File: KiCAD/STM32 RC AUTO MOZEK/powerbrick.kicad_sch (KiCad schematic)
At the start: 3 parts, among them J1 Conn_01x02_Socket, U1 LD1117S33TR_SOT223, U3 L7805

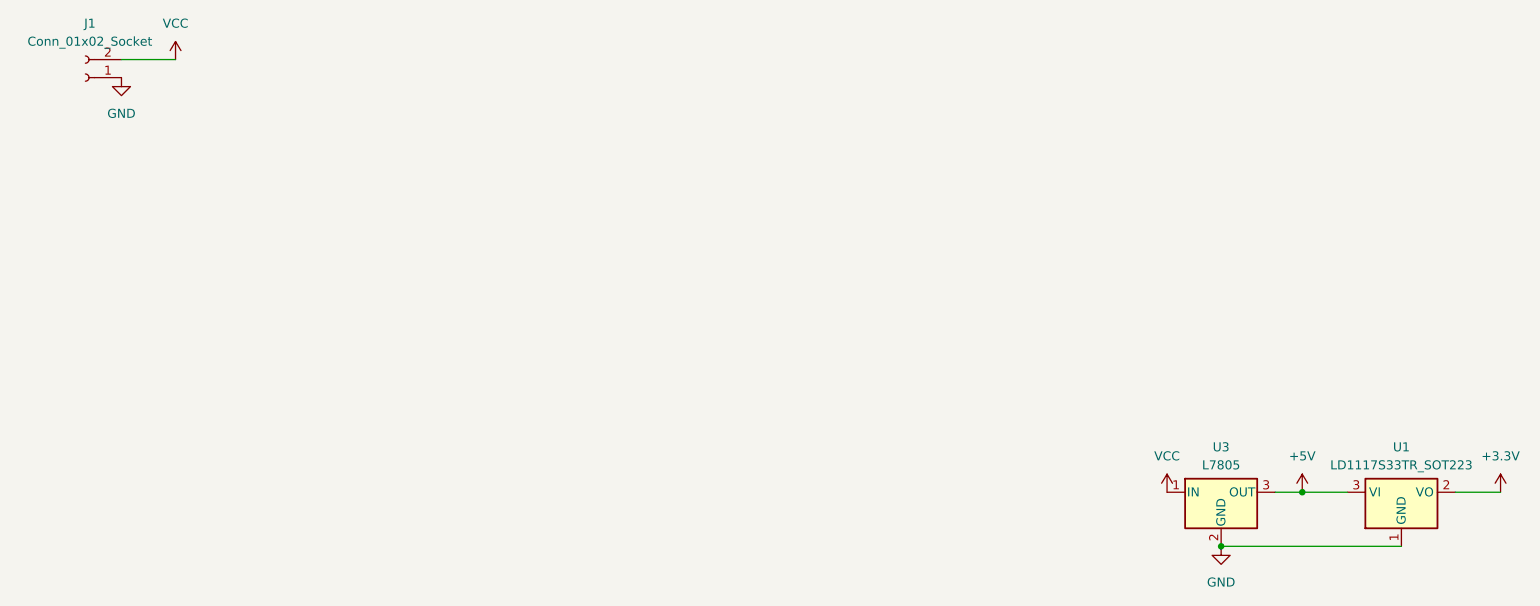
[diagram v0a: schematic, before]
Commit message: adding completation on schematic, working on board
need to add SWD Debug as input for programing
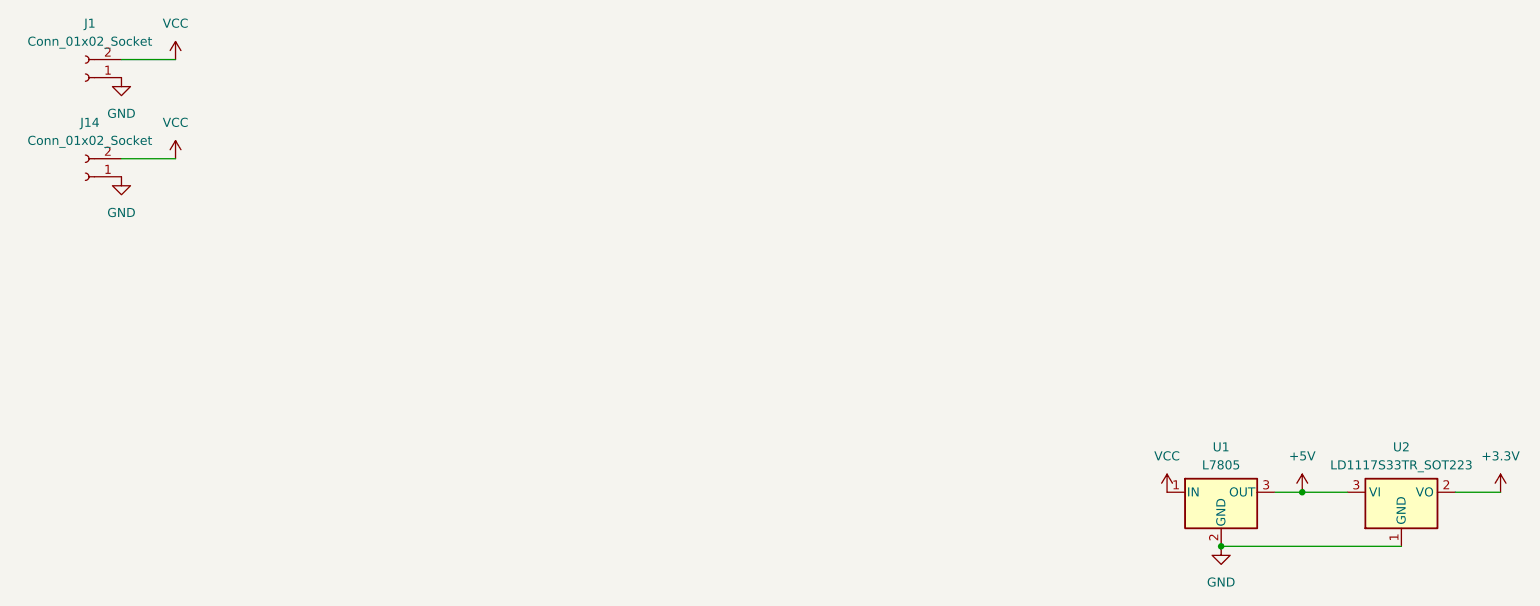
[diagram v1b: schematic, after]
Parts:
- added J14: Conn_01x02_Socket, Connector_Wire:SolderWire-2sqmm_1x02_P7.8mm_D2mm_OD3.9mm, symbol Connector:Conn_01x02_Socket
- J1: footprint Connector_Wire:SolderWire-2sqmm_1x02_P7.8mm_D2mm_OD3.9mm_Relief -> Connector_Wire:SolderWire-2sqmm_1x02_P7.8mm_D2mm_OD3.9mm
- renumbered U3 to U1, U1 to U2
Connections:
- net GND: now also J14.1 (Pin_1)
- net VCC: now also J14.2 (Pin_2)
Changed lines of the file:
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@@
+	(wire
+		(pts
+			(xy 35.56 34.29) (xy 27.94 34.29)
+		)
+		(stroke
+			(width 0)
+			(type default)
+		)
+	)
 	(wire
 		(pts
@@
 	)
 	(symbol
+		(lib_id "power:VCC")
+		(at 35.56 34.29 0)
+		(unit 1)
+		(exclude_from_sim no)
+		(in_bom yes)
+		(on_board yes)
+		(dnp no)
+		(fields_autoplaced yes)
+		(property "Reference" "#PWR086"
+			(at 35.56 38.1 0)
+			(effects
+				(font
+					(size 1.27 1.27)
+				)
+				(hide yes)
+			)
+		)
+		(property "Value" "VCC"
+			(at 35.56 29.21 0)
+			(effects
+				(font
+					(size 1.27 1.27)
+				)
+			)
+		)
+		(property "Footprint" ""
+			(at 35.56 34.29 0)
+			(effects
+				(font
+					(size 1.27 1.27)
+				)
+				(hide yes)
+			)
+		)
+		(property "Datasheet" ""
+			(at 35.56 34.29 0)
+			(effects
+				(font
+					(size 1.27 1.27)
+				)
+				(hide yes)
+			)
+		)
+		(property "Description" "Power symbol creates a global label with name \"VCC\""
+			(at 35.56 34.29 0)
+			(effects
+				(font
+					(size 1.27 1.27)
+				)
+				(hide yes)
+			)
+		)
+		(pin "1"
+		)
+		(instances
+			(project "STM32 RC AUTO MOZEK"
+				(path "/6e2a7673-a3dd-4427-9adf-f28c7cc113a0/dfd97a23-616e-451f-b7bb-3bcde87fded7"
+					(reference "#PWR086")
+					(unit 1)
+				)
+			)
+		)
+	)
+	(symbol
 		(lib_id "power:+5V")
 		(at 194.31 81.28 0)
@@
 		(dnp no)
 		(fields_autoplaced yes)
-		(property "Reference" "#PWR06"
+		(property "Reference" "#PWR05"
 			(at 194.31 85.09 0)
 			(effects
@@
 			(project ""
 				(path "/6e2a7673-a3dd-4427-9adf-f28c7cc113a0/dfd97a23-616e-451f-b7bb-3bcde87fded7"
-					(reference "#PWR06")
+					(reference "#PWR05")
 					(unit 1)
 				)
@@
 		(dnp no)
 		(fields_autoplaced yes)
-		(property "Reference" "U3"
+		(property "Reference" "U1"
 			(at 182.88 74.93 0)
 			(effects
@@
 			(project ""
 				(path "/6e2a7673-a3dd-4427-9adf-f28c7cc113a0/dfd97a23-616e-451f-b7bb-3bcde87fded7"
-					(reference "U3")
+					(reference "U1")
 					(unit 1)
 				)
@@
 		(dnp no)
 		(fields_autoplaced yes)
-		(property "Reference" "U1"
+		(property "Reference" "U2"
 			(at 208.28 74.93 0)
 			(effects
@@
 			(project ""
 				(path "/6e2a7673-a3dd-4427-9adf-f28c7cc113a0/dfd97a23-616e-451f-b7bb-3bcde87fded7"
-					(reference "U1")
+					(reference "U2")
+					(unit 1)
+				)
+			)
+		)
+	)
+	(symbol
+		(lib_id "power:GND")
+		(at 27.94 36.83 0)
+		(unit 1)
+		(exclude_from_sim no)
+		(in_bom yes)
+		(on_board yes)
+		(dnp no)
+		(fields_autoplaced yes)
+		(property "Reference" "#PWR085"
+			(at 27.94 43.18 0)
+			(effects
+				(font
+					(size 1.27 1.27)
+				)
+				(hide yes)
+			)
+		)
+		(property "Value" "GND"
+			(at 27.94 41.91 0)
+			(effects
+				(font
+					(size 1.27 1.27)
+				)
+			)
+		)
+		(property "Footprint" ""
+			(at 27.94 36.83 0)
+			(effects
+				(font
+					(size 1.27 1.27)
+				)
+				(hide yes)
+			)
+		)
+		(property "Datasheet" ""
+			(at 27.94 36.83 0)
+			(effects
+				(font
+					(size 1.27 1.27)
+				)
+				(hide yes)
+			)
+		)
+		(property "Description" "Power symbol creates a global label with name \"GND\" , ground"
+			(at 27.94 36.83 0)
+			(effects
+				(font
+					(size 1.27 1.27)
+				)
+				(hide yes)
+			)
+		)
+		(pin "1"
+		)
+		(instances
+			(project "STM32 RC AUTO MOZEK"
+				(path "/6e2a7673-a3dd-4427-9adf-f28c7cc113a0/dfd97a23-616e-451f-b7bb-3bcde87fded7"
+					(reference "#PWR085")
 					(unit 1)
 				)
@@
 		(dnp no)
 		(fields_autoplaced yes)
-		(property "Reference" "#PWR013"
+		(property "Reference" "#PWR03"
 			(at 175.26 85.09 0)
 			(effects
@@
 			(project "STM32 RC AUTO MOZEK"
 				(path "/6e2a7673-a3dd-4427-9adf-f28c7cc113a0/dfd97a23-616e-451f-b7bb-3bcde87fded7"
-					(reference "#PWR013")
+					(reference "#PWR03")
 					(unit 1)
 				)
@@
 		(dnp no)
 		(fields_autoplaced yes)
-		(property "Reference" "#PWR08"
+		(property "Reference" "#PWR02"
 			(at 35.56 24.13 0)
 			(effects
@@
 			(project ""
 				(path "/6e2a7673-a3dd-4427-9adf-f28c7cc113a0/dfd97a23-616e-451f-b7bb-3bcde87fded7"
-					(reference "#PWR08")
+					(reference "#PWR02")
 					(unit 1)
 				)
@@
 		(dnp no)
 		(fields_autoplaced yes)
-		(property "Reference" "#PWR09"
+		(property "Reference" "#PWR01"
 			(at 27.94 29.21 0)
 			(effects
@@
 			(project ""
 				(path "/6e2a7673-a3dd-4427-9adf-f28c7cc113a0/dfd97a23-616e-451f-b7bb-3bcde87fded7"
-					(reference "#PWR09")
+					(reference "#PWR01")
 					(unit 1)
 				)
@@
 		(dnp no)
 		(fields_autoplaced yes)
-		(property "Reference" "#PWR05"
+		(property "Reference" "#PWR06"
 			(at 222.25 85.09 0)
 			(effects
@@
 			(project ""
 				(path "/6e2a7673-a3dd-4427-9adf-f28c7cc113a0/dfd97a23-616e-451f-b7bb-3bcde87fded7"
-					(reference "#PWR05")
+					(reference "#PWR06")
 					(unit 1)
 				)
@@
 			)
 		)
-		(property "Footprint" "Connector_Wire:SolderWire-2sqmm_1x02_P7.8mm_D2mm_OD3.9mm_Relief"
+		(property "Footprint" "Connector_Wire:SolderWire-2sqmm_1x02_P7.8mm_D2mm_OD3.9mm"
 			(at 22.86 22.86 0)
 			(effects
@@
 	)
 	(symbol
+		(lib_id "Connector:Conn_01x02_Socket")
+		(at 22.86 36.83 180)
+		(unit 1)
+		(exclude_from_sim no)
+		(in_bom yes)
+		(on_board yes)
+		(dnp no)
+		(fields_autoplaced yes)
+		(property "Reference" "J14"
+			(at 23.495 29.21 0)
+			(effects
+				(font
+					(size 1.27 1.27)
+				)
+			)
+		)
+		(property "Value" "Conn_01x02_Socket"
+			(at 23.495 31.75 0)
+			(effects
+				(font
+					(size 1.27 1.27)
+				)
+			)
+		)
+		(property "Footprint" "Connector_Wire:SolderWire-2sqmm_1x02_P7.8mm_D2mm_OD3.9mm"
+			(at 22.86 36.83 0)
+			(effects
+				(font
+					(size 1.27 1.27)
+				)
+				(hide yes)
+			)
+		)
+		(property "Datasheet" "~"
+			(at 22.86 36.83 0)
+			(effects
+				(font
+					(size 1.27 1.27)
+				)
+				(hide yes)
+			)
+		)
+		(property "Description" "Generic connector, single row, 01x02, script generated"
+			(at 22.86 36.83 0)
+			(effects
+				(font
+					(size 1.27 1.27)
+				)
+				(hide yes)
+			)
+		)
+		(pin "1"
+		)
+		(pin "2"
+		)
+		(instances
+			(project "STM32 RC AUTO MOZEK"
+				(path "/6e2a7673-a3dd-4427-9adf-f28c7cc113a0/dfd97a23-616e-451f-b7bb-3bcde87fded7"
+					(reference "J14")
+					(unit 1)
+				)
+			)
+		)
+	)
+	(symbol
 		(lib_id "power:GND")
 		(at 182.88 88.9 0)
@@
 		(dnp no)
 		(fields_autoplaced yes)
-		(property "Reference" "#PWR010"
+		(property "Reference" "#PWR04"
 			(at 182.88 95.25 0)
 			(effects
@@
 			(project "STM32 RC AUTO MOZEK"
 				(path "/6e2a7673-a3dd-4427-9adf-f28c7cc113a0/dfd97a23-616e-451f-b7bb-3bcde87fded7"
-					(reference "#PWR010")
-					(unit 1)
-				)
+					(reference "#PWR04")
+					(unit 1)
+				)

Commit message: .
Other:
- moved on the sheet: U1, U2
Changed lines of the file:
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@@
 	(paper "A4")
 	(junction
-		(at 182.88 88.9)
+		(at 67.31 36.83)
 		(diameter 0)
 		(color 0 0 0 0)
 	)
 	(junction
-		(at 194.31 81.28)
+		(at 78.74 29.21)
 		(diameter 0)
 		(color 0 0 0 0)
@@
 	(wire
 		(pts
-			(xy 194.31 81.28) (xy 200.66 81.28)
+			(xy 78.74 29.21) (xy 85.09 29.21)
 		)
 		(stroke
@@
 	(wire
 		(pts
-			(xy 182.88 88.9) (xy 208.28 88.9)
+			(xy 67.31 36.83) (xy 92.71 36.83)
 		)
 		(stroke
@@
 	(wire
 		(pts
-			(xy 222.25 81.28) (xy 215.9 81.28)
+			(xy 106.68 29.21) (xy 100.33 29.21)
 		)
 		(stroke
@@
 	(wire
 		(pts
-			(xy 190.5 81.28) (xy 194.31 81.28)
+			(xy 74.93 29.21) (xy 78.74 29.21)
 		)
 		(stroke
@@
 	(symbol
 		(lib_id "power:+5V")
-		(at 194.31 81.28 0)
+		(at 78.74 29.21 0)
 		(unit 1)
 		(exclude_from_sim no)
@@
 		(fields_autoplaced yes)
 		(property "Reference" "#PWR05"
-			(at 194.31 85.09 0)
+			(at 78.74 33.02 0)
 			(effects
 				(font
@@
 		)
 		(property "Value" "+5V"
-			(at 194.31 76.2 0)
+			(at 78.74 24.13 0)
 			(effects
 				(font
@@
 		)
 		(property "Footprint" ""
-			(at 194.31 81.28 0)
+			(at 78.74 29.21 0)
 			(effects
 				(font
@@
 		)
 		(property "Datasheet" ""
-			(at 194.31 81.28 0)
+			(at 78.74 29.21 0)
 			(effects
 				(font
@@
 		)
 		(property "Description" "Power symbol creates a global label with name \"+5V\""
-			(at 194.31 81.28 0)
+			(at 78.74 29.21 0)
 			(effects
 				(font
@@
 	(symbol
 		(lib_id "Regulator_Linear:L7805")
-		(at 182.88 81.28 0)
+		(at 67.31 29.21 0)
 		(unit 1)
 		(exclude_from_sim no)
@@
 		(fields_autoplaced yes)
 		(property "Reference" "U1"
-			(at 182.88 74.93 0)
+			(at 67.31 22.86 0)
 			(effects
 				(font
@@
 		)
 		(property "Value" "L7805"
-			(at 182.88 77.47 0)
+			(at 67.31 25.4 0)
 			(effects
 				(font
@@
 		)
 		(property "Footprint" "Package_TO_SOT_THT:TO-220-3_Horizontal_TabDown"
-			(at 183.515 85.09 0)
+			(at 67.945 33.02 0)
 			(effects
 				(font
@@
 		)
 		(property "Datasheet" "http://www.st.com/content/ccc/resource/technical/document/datasheet/41/4f/b3/b0/12/d4/47/88/CD00000444.pdf/files/CD00000444.pdf/jcr:content/translations/en.CD00000444.pdf"
-			(at 182.88 82.55 0)
+			(at 67.31 30.48 0)
 			(effects
 				(font
@@
 		)
 		(property "Description" "Positive 1.5A 35V Linear Regulator, Fixed Output 5V, TO-220/TO-263/TO-252"
-			(at 182.88 81.28 0)
+			(at 67.31 29.21 0)
 			(effects
 				(font
@@
 	(symbol
 		(lib_id "Regulator_Linear:LD1117S33TR_SOT223")
-		(at 208.28 81.28 0)
+		(at 92.71 29.21 0)
 		(unit 1)
 		(exclude_from_sim no)
@@
 		(fields_autoplaced yes)
 		(property "Reference" "U2"
-			(at 208.28 74.93 0)
+			(at 92.71 22.86 0)
 			(effects
 				(font
@@
 		)
 		(property "Value" "LD1117S33TR_SOT223"
-			(at 208.28 77.47 0)
+			(at 92.71 25.4 0)
 			(effects
 				(font
@@
 		)
 		(property "Footprint" "Package_TO_SOT_SMD:SOT-223-3_TabPin2"
-			(at 208.28 76.2 0)
+			(at 92.71 24.13 0)
 			(effects
 				(font
@@
 		)
 		(property "Datasheet" "http://www.st.com/st-web-ui/static/active/en/resource/technical/document/datasheet/CD00000544.pdf"
-			(at 210.82 87.63 0)
+			(at 95.25 35.56 0)
 			(effects
 				(font
@@
 		)
 		(property "Description" "800mA Fixed Low Drop Positive Voltage Regulator, Fixed Output 3.3V, SOT-223"
-			(at 208.28 81.28 0)
+			(at 92.71 29.21 0)
 			(effects
 				(font
@@
 	(symbol
 		(lib_id "power:VCC")
-		(at 175.26 81.28 0)
+		(at 59.69 29.21 0)
 		(unit 1)
 		(exclude_from_sim no)
@@
 		(fields_autoplaced yes)
 		(property "Reference" "#PWR03"
-			(at 175.26 85.09 0)
+			(at 59.69 33.02 0)
 			(effects
 				(font
@@
 		)
 		(property "Value" "VCC"
-			(at 175.26 76.2 0)
+			(at 59.69 24.13 0)
 			(effects
 				(font
@@
 		)
 		(property "Footprint" ""
-			(at 175.26 81.28 0)
+			(at 59.69 29.21 0)
 			(effects
 				(font
@@
 		)
 		(property "Datasheet" ""
-			(at 175.26 81.28 0)
+			(at 59.69 29.21 0)
 			(effects
 				(font
@@
 		)
 		(property "Description" "Power symbol creates a global label with name \"VCC\""
-			(at 175.26 81.28 0)
+			(at 59.69 29.21 0)
 			(effects
 				(font
@@
 	(symbol
 		(lib_id "power:+3.3V")
-		(at 222.25 81.28 0)
+		(at 106.68 29.21 0)
 		(unit 1)
 		(exclude_from_sim no)
@@
 		(fields_autoplaced yes)
 		(property "Reference" "#PWR06"
-			(at 222.25 85.09 0)
+			(at 106.68 33.02 0)
 			(effects
 				(font
@@
 		)
 		(property "Value" "+3.3V"
-			(at 222.25 76.2 0)
+			(at 106.68 24.13 0)
 			(effects
 				(font
@@
 		)
 		(property "Footprint" ""
-			(at 222.25 81.28 0)
+			(at 106.68 29.21 0)
 			(effects
 				(font
@@
 		)
 		(property "Datasheet" ""
-			(at 222.25 81.28 0)
+			(at 106.68 29.21 0)
 			(effects
 				(font
@@
 		)
 		(property "Description" "Power symbol creates a global label with name \"+3.3V\""
-			(at 222.25 81.28 0)
+			(at 106.68 29.21 0)
 			(effects
 				(font
@@
 	(symbol
 		(lib_id "power:GND")
-		(at 182.88 88.9 0)
+		(at 67.31 36.83 0)
 		(unit 1)
 		(exclude_from_sim no)
@@
 		(fields_autoplaced yes)
 		(property "Reference" "#PWR04"
-			(at 182.88 95.25 0)
+			(at 67.31 43.18 0)
 			(effects
 				(font
@@
 		)
 		(property "Value" "GND"
-			(at 182.88 93.98 0)
+			(at 67.31 41.91 0)
 			(effects
 				(font
@@
 		)
 		(property "Footprint" ""
-			(at 182.88 88.9 0)
+			(at 67.31 36.83 0)
 			(effects
 				(font
@@
 		)
 		(property "Datasheet" ""
-			(at 182.88 88.9 0)
+			(at 67.31 36.83 0)
 			(effects
 				(font
@@
 		)
 		(property "Description" "Power symbol creates a global label with name \"GND\" , ground"
-			(at 182.88 88.9 0)
-			(effects
-				(font
+			(at 67.31 36.83 0)
+			(effects
+				(font
